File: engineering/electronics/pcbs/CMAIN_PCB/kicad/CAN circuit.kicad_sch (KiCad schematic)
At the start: 17 parts, among them U1 TJA1049T/3J, U2 MCP2515-I/SO, X1 16MHz

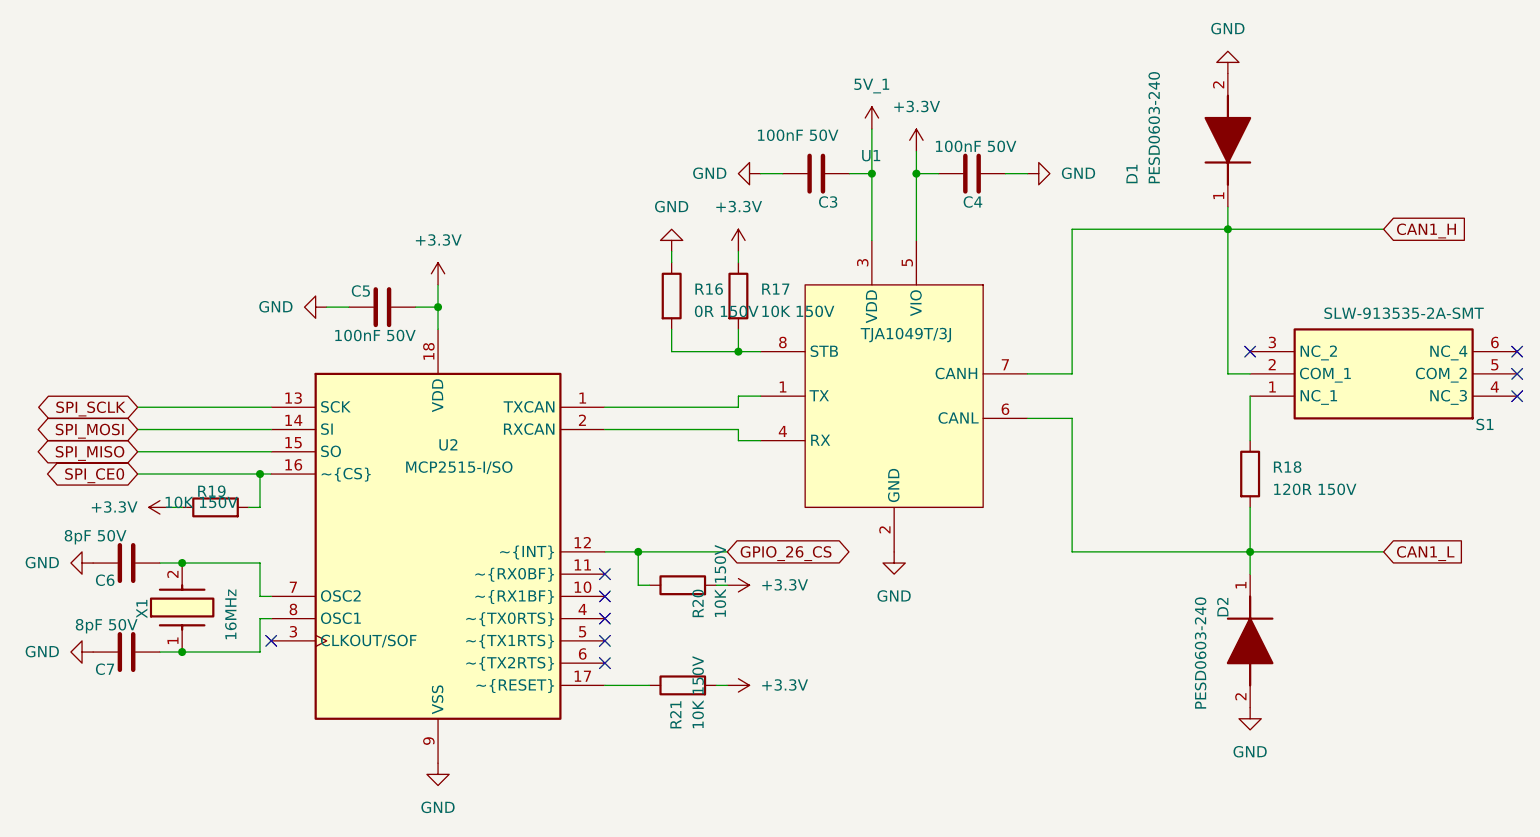
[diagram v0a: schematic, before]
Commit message: fix(cmain): integrate prototype ordering update
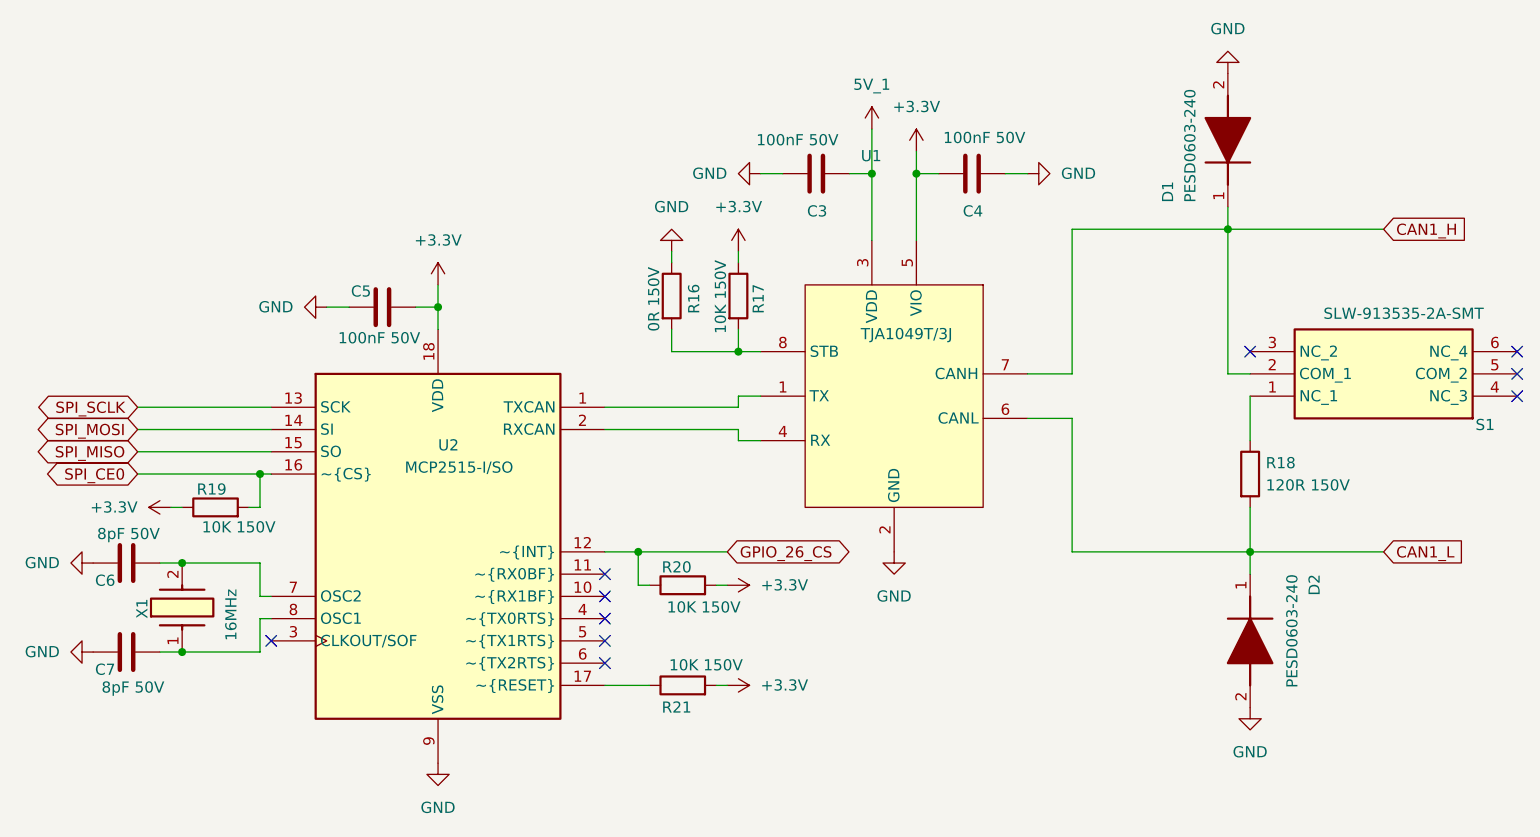
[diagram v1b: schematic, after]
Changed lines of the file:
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@@
 		(dnp no)
 		(property "Reference" "R19"
-			(at 92.71 102.87 90)
+			(at 92.71 102.616 90)
 			(show_name no)
 			(do_not_autoplace no)
@@
 		)
 		(property "Value" "10K 150V"
-			(at 93.98 104.14 90)
+			(at 98.298 106.934 90)
 			(show_name no)
 			(do_not_autoplace no)
@@
 		)
 		(property "Value" "8pF 50V"
-			(at 82.55 118.11 90)
+			(at 85.598 125.222 90)
 			(show_name no)
 			(do_not_autoplace no)
@@
 		(dnp no)
 		(property "Reference" "C3"
-			(at 162.56 69.85 90)
+			(at 161.29 70.866 90)
 			(show_name no)
 			(do_not_autoplace no)
@@
 		)
 		(property "Value" "100nF 50V"
-			(at 162.56 62.23 90)
+			(at 162.56 62.738 90)
 			(show_name no)
 			(do_not_autoplace no)
@@
 		(dnp no)
 		(property "Reference" "C4"
-			(at 179.07 69.85 90)
+			(at 179.07 70.866 90)
 			(show_name no)
 			(do_not_autoplace no)
@@
 		)
 		(property "Value" "100nF 50V"
-			(at 182.88 63.5 90)
+			(at 183.896 62.484 90)
 			(show_name no)
 			(do_not_autoplace no)
@@
 		(dnp no)
 		(property "Reference" "R20"
-			(at 147.32 118.11 0)
+			(at 145.796 111.506 90)
 			(show_name no)
 			(do_not_autoplace no)
@@
 		)
 		(property "Value" "10K 150V"
-			(at 149.86 118.11 0)
+			(at 151.384 116.078 90)
 			(show_name no)
 			(do_not_autoplace no)
@@
 		(dnp no)
 		(property "Reference" "D2"
-			(at 205.74 115.57 0)
+			(at 216.154 113.03 0)
 			(show_name no)
 			(do_not_autoplace no)
@@
 		)
 		(property "Value" "PESD0603-240"
-			(at 203.2 115.57 0)
+			(at 213.614 113.03 0)
 			(show_name no)
 			(do_not_autoplace no)
@@
 		(dnp no)
 		(property "Reference" "R17"
-			(at 153.67 81.28 0)
+			(at 154.178 83.312 90)
 			(show_name no)
 			(do_not_autoplace no)
@@
 		)
 		(property "Value" "10K 150V"
-			(at 153.67 83.82 0)
+			(at 149.86 85.598 90)
 			(show_name no)
 			(do_not_autoplace no)
@@
 		(dnp no)
 		(property "Reference" "D1"
-			(at 196.85 68.58 0)
+			(at 200.914 70.612 0)
 			(show_name no)
 			(do_not_autoplace no)
@@
 		)
 		(property "Value" "PESD0603-240"
-			(at 199.39 68.58 0)
+			(at 203.454 70.612 0)
 			(show_name no)
 			(do_not_autoplace no)
@@
 		(dnp no)
 		(property "Reference" "R18"
-			(at 212.09 101.6 0)
+			(at 211.328 101.092 0)
 			(show_name no)
 			(do_not_autoplace no)
@@
 		)
 		(property "Value" "120R 150V"
-			(at 212.09 104.14 0)
+			(at 211.328 103.632 0)
 			(show_name no)
 			(do_not_autoplace no)
@@
 		(dnp no)
 		(property "Reference" "R16"
-			(at 146.05 81.28 0)
+			(at 146.812 83.312 90)
 			(show_name no)
 			(do_not_autoplace no)
@@
 		)
 		(property "Value" "0R 150V"
-			(at 146.05 83.82 0)
+			(at 142.24 85.344 90)
 			(show_name no)
 			(do_not_autoplace no)
@@
 		(dnp no)
 		(property "Reference" "R21"
-			(at 144.78 130.81 0)
+			(at 145.796 127.508 90)
 			(show_name no)
 			(do_not_autoplace no)
@@
 		)
 		(property "Value" "10K 150V"
-			(at 147.32 130.81 0)
+			(at 151.638 122.682 90)
 			(show_name no)
 			(do_not_autoplace no)
@@
 		)
 		(property "Value" "8pF 50V"
-			(at 81.28 107.95 90)
+			(at 85.09 107.696 90)
 			(show_name no)
 			(do_not_autoplace no)
@@
 		)
 		(property "Value" "100nF 50V"
-			(at 114.3 85.09 90)
+			(at 114.808 85.344 90)
 			(show_name no)
 			(do_not_autoplace no)
